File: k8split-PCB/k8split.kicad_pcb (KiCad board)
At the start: 2 copper layers, 421.6 x 118.7 mm, 233 parts, among them J1 AVR-ISP-6, J13 Breakaway_Tabs, J14 Breakaway_Tabs, J17 Breakaway_Tabs, J18 Breakaway_Tabs, J19 Breakaway_Tabs, J2 AVR-ISP-6, J3 Breakaway_Tabs, J5 Breakaway_Tabs, J6 Breakaway_Tabs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

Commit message: near completed routing on boards
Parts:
- added C6: 0.1uF, Capacitor_SMD:C_0603_1608Metric, B.Cu at (38.1, 129.5)
- added H1: MountingHole, MountingHole:MountingHole_3.2mm_M3, F.Cu at (-61.5, 29.0)
- added H2: MountingHole, MountingHole:MountingHole_3.2mm_M3, F.Cu at (-61.5, 140.7)
- added H3: MountingHole, MountingHole:MountingHole_3.2mm_M3, F.Cu at (88.4, 29.0)
- added H4: MountingHole, MountingHole:MountingHole_3.2mm_M3, F.Cu at (127.5, 140.7)
- added H5: MountingHole, MountingHole:MountingHole_3.2mm_M3, F.Cu at (203.7, 29.0)
- added H6: MountingHole, MountingHole:MountingHole_3.2mm_M3, F.Cu at (164.6, 140.7)
- added H7: MountingHole, MountingHole:MountingHole_3.2mm_M3, F.Cu at (353.6, 29.0)
- added H8: MountingHole, MountingHole:MountingHole_3.2mm_M3, F.Cu at (353.6, 140.7)
- C15, C3, C4, C7: moved to B.Cu
- moved C3 111.7 mm to (19.2, 132.6), turned to 90 degrees
- moved C4 108.8 mm to (26.4, 140.2)
- moved Y1 105.4 mm to (29.0, 122.4), turned to 180 degrees
- moved C7 104.7 mm to (26.4, 125.0), turned to 180 degrees
- moved C1 104.1 mm to (32.0, 122.4), turned to 90 degrees
- moved R25 103.8 mm to (38.1, 137.2), turned to 180 degrees
- moved C2 103.1 mm to (29.0, 119.9)
- moved C15 102.9 mm to (33.0, 140.2)
- moved C9 28.5 mm to (221.5, 120.9), turned to 270 degrees
- moved Y2 22.4 mm to (224.5, 120.9), turned to 180 degrees
- moved C8 16.3 mm to (227.6, 120.9), turned to 90 degrees
- moved D43 5.97 mm to (79.8, 29.8)
- moved R1 4.83 mm to (115.8, 107.2)
- moved SW1 3.09 mm to (120.0, 114.7)
- moved J1 3.09 mm to (120.0, 107.1)
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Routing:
- net GNDA: track 403.1 -> 9.36 mm, vias 8 -> 6
- net +5V: track 10.8 -> 323.5 mm, vias 0 -> 5
- net D-: track 0.00 -> 190.5 mm
- net D+: track 0.00 -> 189.7 mm
- net SCK: track 0.00 -> 124.1 mm, vias 0 -> 2
- net MISO: track 0.00 -> 119.7 mm, vias 0 -> 2
- net MOSI: track 0.00 -> 117.3 mm, vias 0 -> 2
- net RESET: track 8.23 -> 117.7 mm, vias 0 -> 3
- net ROW0: track 148.2 -> 253.2 mm, vias 0 -> 2
- net ROW1: track 133.3 -> 225.5 mm, vias 0 -> 2
- net COL0: track 103.1 -> 194.4 mm, vias 0 -> 1
- net COL7: track 111.2 -> 194.1 mm
- net ROW2: track 137.8 -> 212.1 mm, vias 0 -> 2
- net COL6: track 111.2 -> 178.6 mm, vias 0 -> 1
- net COL1: track 111.0 -> 178.3 mm, vias 0 -> 1
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- added copper zone on B.Cu, net GND
- added copper zone on F.Cu, net GND
- added copper zone on B.Cu, net GNDA
- added copper zone on F.Cu, net GNDA
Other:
- board size 421.6 x 118.7 mm -> 421.6 x 124.8 mm

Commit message: add some branding to pcb
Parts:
- added G***: LOGO, cad:pppp, B.Cu at (-58.6, 127.7)
- added G***: LOGO, cad:ppp, B.Cu at (350.9, 127.7)
- added G***: LOGO, cad:right, F.Cu at (291.6, 84.8)
- added G***: LOGO, cad:left, F.Cu at (0.51, 84.8)
- renumbered SW2 to RST, SW1 to RST
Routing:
- net Net-(D13-Pad2): track 0.00 -> 3.28 mm
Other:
- board text added: "https://github.com/ckath/k8split"

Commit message: small board redesign regarding usb, start fixing silkscreen
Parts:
- moved H1 2.54 mm to (-63.0, 26.9)
- moved G*** 2.30 mm to (-60.6, 128.9)
- moved H7 2.27 mm to (354.6, 26.9)
- moved H3 2.27 mm to (89.4, 26.9)
- moved H5 2.27 mm to (202.7, 26.9)
- moved H2 1.83 mm to (-63.0, 141.7)
- moved G*** 1.70 mm to (352.2, 128.8)
- moved H6 1.44 mm to (163.6, 141.7)
- moved H8 1.44 mm to (354.6, 141.7)
- moved H4 1.44 mm to (128.5, 141.7)
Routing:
- net D-: track 190.5 -> 191.3 mm
- net D+: track 189.7 -> 190.6 mm
- net GND: vias 4 -> 3
- net (no net): vias 0 -> 1
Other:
- board size 421.6 x 124.8 mm -> 424.7 x 121.9 mm
- board text added: "GITHUB.COM/CKATH/K8SPLIT"
- board text removed: "https://github.com/ckath/k8split"

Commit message: initial panelizing
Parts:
- removed J13, J14, J17, J18, J19: Breakaway_Tabs, locallib:breakaway-mousebites
- removed RST: SW_Push, locallib:SKQGADE010
- added J4: Breakaway_Tabs, locallib:breakaway-mousebites, F.Cu at (132.6, 142.0)
- added J8: Breakaway_Tabs, locallib:breakaway-mousebites, F.Cu at (89.7, 22.9)
- added SW2: SW_Push, locallib:SKQGADE010, F.Cu at (158.5, 79.4)
- moved J3 383.3 mm to (-43.7, 21.1)
- moved J5 212.0 mm to (108.5, 90.7), turned to 90 degrees
- moved J9 190.3 mm to (175.0, 22.6), turned to 180 degrees
- moved J6 184.9 mm to (147.6, 90.7), turned to 90 degrees
- moved J7 149.1 mm to (308.9, 20.8)
- moved G*** 34.0 mm to (257.6, 84.8)
- moved C10 27.4 mm to (188.5, 132.6)
- moved C11 27.4 mm to (193.0, 140.2)
- moved C16 27.4 mm to (200.2, 140.2)
- moved C8 27.4 mm to (200.2, 120.9)
- moved D49 27.4 mm to (190.4, 29.8)
- moved D52 27.4 mm to (166.2, 87.6)
- moved D53 27.4 mm to (156.7, 106.7)
- moved D54 27.4 mm to (152.3, 125.7)
- moved D56 27.4 mm to (190.4, 48.9)
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- renumbered RST to SW1
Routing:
- net SCK: track 124.1 -> 125.3 mm
- net GNDA: track 9.36 -> 10.4 mm
- net GND: vias 3 -> 5
- net (no net): vias 1 -> 0
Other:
- board size 424.7 x 121.9 mm -> 397.3 x 131.3 mm
- board text added: "JLCJLCJLCJLC"
- board text added: "rev 0.1"

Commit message: finish panelizing pcb
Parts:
- moved J7 160.6 mm to (151.6, 53.3), turned to 270 degrees
- moved J3 141.1 mm to (93.7, 53.3), turned to 90 degrees
- moved J9 5.75 mm to (170.9, 26.7), turned to 270 degrees
- moved J8 5.57 mm to (93.7, 26.7), turned to 90 degrees
- moved J6 0.51 mm to (147.1, 90.7), turned to 270 degrees
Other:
- board size 397.3 x 131.3 mm -> 397.3 x 124 mm
- board text added: "K 8 S P L I T R0.1"
- board text added: "initial release"

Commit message: initial gerber files
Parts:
- moved R67 2.40 mm to (204.7, 138.9)
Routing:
- net COL7-R: track 230.9 -> 229.6 mm
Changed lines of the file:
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@@
   (general
     (thickness 1.6)
-    (drawings 58)
-    (tracks 1130)
+    (drawings 60)
+    (tracks 1133)
     (zones 0)
     (modules 243)
@@
       (drillshape 0)
       (scaleselection 1)
-      (outputdirectory "Position"))
+      (outputdirectory "Gerber"))
   )
   (net 0 "")
@@
   )
   (module Resistor_SMD:R_0805_2012Metric (layer B.Cu)
-    (at 202.692 140.208 90)
+    (at 204.724 138.938 90)
     (descr "Resistor SMD 0805 (2012 Metric), square (rectangular) end terminal, IPC_7351 nominal, (Body size source: https://docs.google.com/spreadsheets/d/1BsfQQcO9C6DZCsRaXUlFlo91Tg2WpOkGARC1WS5S8t0/edit?usp=sharing), generated with kicad-footprint-generator")
     (tags resistor)
     (attr smd)
-    (fp_text reference R67 (at -2.54 0.508 180) (layer B.SilkS)
+    (fp_text reference R67 (at -2.54 0 180) (layer B.SilkS)
       (effects (font (size 1 1) (thickness 0.15)) (justify mirror))
     )
@@
   (module locallib:SKQGADE010 (layer F.Cu)
     (at 158.496 79.375)
-    (fp_text reference SW2 (at 0 4.064) (layer F.SilkS)
+    (fp_text reference SW2 (at 0 4.064) (layer F.SilkS) hide
       (effects (font (size 1 1) (thickness 0.15)))
     )
@@
   (module locallib:SKQGADE010 (layer F.Cu)
     (at 120.015 114.681)
-    (fp_text reference SW1 (at 0 3.81) (layer F.SilkS)
+    (fp_text reference SW1 (at 0 3.81) (layer F.SilkS) hide
       (effects (font (size 1 1) (thickness 0.15)))
     )
@@
     )
   )
+  (dimension 123.952 (width 0.15) (layer Dwgs.User)
+    (gr_text "123.952 mm" (at 342.422 83.312 90) (layer Dwgs.User)
+      (effects (font (size 1 1) (thickness 0.15)))
+    )
+    (feature1 (pts (xy 330.708 21.336) (xy 341.708421 21.336)))
+    (feature2 (pts (xy 330.708 145.288) (xy 341.708421 145.288)))
+    (crossbar (pts (xy 341.122 145.288) (xy 341.122 21.336)))
+    (arrow1a (pts (xy 341.122 21.336) (xy 341.708421 22.462504)))
+    (arrow1b (pts (xy 341.122 21.336) (xy 340.535579 22.462504)))
+    (arrow2a (pts (xy 341.122 145.288) (xy 341.708421 144.161496)))
+    (arrow2b (pts (xy 341.122 145.288) (xy 340.535579 144.161496)))
+  )
+  (dimension 397.256 (width 0.15) (layer Dwgs.User)
+    (gr_text "397.256 mm" (at 132.08 6.574001) (layer Dwgs.User)
+      (effects (font (size 1 1) (thickness 0.15)))
+    )
+    (feature1 (pts (xy -66.548 23.368) (xy -66.548 7.28758)))
+    (feature2 (pts (xy 330.708 23.368) (xy 330.708 7.28758)))
+    (crossbar (pts (xy 330.708 7.874001) (xy -66.548 7.874001)))
+    (arrow1a (pts (xy -66.548 7.874001) (xy -65.421496 7.28758)))
+    (arrow1b (pts (xy -66.548 7.874001) (xy -65.421496 8.460422)))
+    (arrow2a (pts (xy 330.708 7.874001) (xy 329.581496 7.28758)))
+    (arrow2b (pts (xy 330.708 7.874001) (xy 329.581496 8.460422)))
+  )
   (gr_text "initial release" (at 122.174 53.34) (layer F.SilkS)
     (effects (font (size 4 4) (thickness 0.5)))
@@
   (via (at 202.692 120.396) (size 0.8) (drill 0.4) (layers F.Cu B.Cu) (net 6))
   (via (at 195.58 123.444) (size 0.8) (drill 0.4) (layers F.Cu B.Cu) (net 6))
-  (via (at 204.216 140.208) (size 0.8) (drill 0.4) (layers F.Cu B.Cu) (net 6))
+  (via (at 203.708 141.478) (size 0.8) (drill 0.4) (layers F.Cu B.Cu) (net 6))
   (segment (start 188.1325 133.515) (end 189.892 133.515) (width 0.381) (layer B.Cu) (net 6))
   (segment (start 187.6805 133.063) (end 188.1325 133.515) (width 0.381) (layer B.Cu) (net 6))
@@
   (segment (start 304.416363 53.373325) (end 304.416363 67.681671) (width 0.254) (layer F.Cu) (net 140) (status 10))
   (segment (start 297.253524 117.720258) (end 309.102442 129.569176) (width 0.254) (layer F.Cu) (net 140) (status 20))
-  (segment (start 292.1 139.192) (end 205.232 139.192) (width 0.254) (layer B.Cu) (net 140))
   (segment (start 301.722824 129.569176) (end 309.102442 129.569176) (width 0.254) (layer B.Cu) (net 140) (status 20))
   (segment (start 292.1 139.192) (end 301.722824 129.569176) (width 0.254) (layer B.Cu) (net 140))
   (via (at 204.216 130.302) (size 0.8) (drill 0.4) (layers F.Cu B.Cu) (net 140))
-  (segment (start 204.203 130.315) (end 204.216 130.302) (width 0.254) (layer B.Cu) (net 140))
-  (segment (start 202.423 130.315) (end 204.203 130.315) (width 0.254) (layer B.Cu) (net 140) (status 10))
-  (segment (start 204.216 130.302) (end 204.216 138.176) (width 0.254) (layer F.Cu) (net 140))
-  (segment (start 204.216 138.176) (end 205.232 139.192) (width 0.254) (layer F.Cu) (net 140))
-  (via (at 205.232 139.192) (size 0.8) (drill 0.4) (layers F.Cu B.Cu) (net 140))
+  (via (at 204.978 136.144) (size 0.8) (drill 0.4) (layers F.Cu B.Cu) (net 140))
+  (segment (start 208.026 139.192) (end 204.978 136.144) (width 0.254) (layer B.Cu) (net 140))
+  (segment (start 292.1 139.192) (end 208.026 139.192) (width 0.254) (layer B.Cu) (net 140))
+  (segment (start 202.436 130.302) (end 202.423 130.315) (width 0.254) (layer B.Cu) (net 140))
+  (segment (start 204.216 130.302) (end 202.436 130.302) (width 0.254) (layer B.Cu) (net 140))
+  (segment (start 204.578001 135.744001) (end 204.978 136.144) (width 0.254) (layer F.Cu) (net 140))
+  (segment (start 203.816001 130.701999) (end 203.816001 134.982001) (width 0.254) (layer F.Cu) (net 140))
+  (segment (start 203.816001 134.982001) (end 204.578001 135.744001) (width 0.254) (layer F.Cu) (net 140))
+  (segment (start 204.216 130.302) (end 203.816001 130.701999) (width 0.254) (layer F.Cu) (net 140))
   (segment (start -44.744 32.0425) (end -44.704 32.0825) (width 0.254) (layer B.Cu) (net 141) (status 30))
   (segment (start -44.744 29.464) (end -44.744 32.0425) (width 0.254) (layer B.Cu) (net 141) (status 30))
@@
   (segment (start 36.5905 136.588) (end 37.1625 137.16) (width 0.254) (layer B.Cu) (net 147) (status 20))
   (segment (start 35.418 136.588) (end 36.5905 136.588) (width 0.254) (layer B.Cu) (net 147) (status 10))
-  (segment (start 202.423 139.0015) (end 202.692 139.2705) (width 0.254) (layer B.Cu) (net 148) (status 30))
-  (segment (start 202.423 136.715) (end 202.423 139.0015) (width 0.254) (layer B.Cu) (net 148) (status 30))
+  (segment (start 203.4385 136.715) (end 202.423 136.715) (width 0.254) (layer B.Cu) (net 148))
+  (segment (start 204.724 138.0005) (end 203.4385 136.715) (width 0.254) (layer B.Cu) (net 148))
   (segment (start 253.893267 69.595) (end 253.594201 69.894066) (width 0.254) (layer B.Cu) (net 167) (status 30))
   (segment (start 257.048 69.595) (end 253.893267 69.595) (width 0.254) (layer B.Cu) (net 167) (status 30))

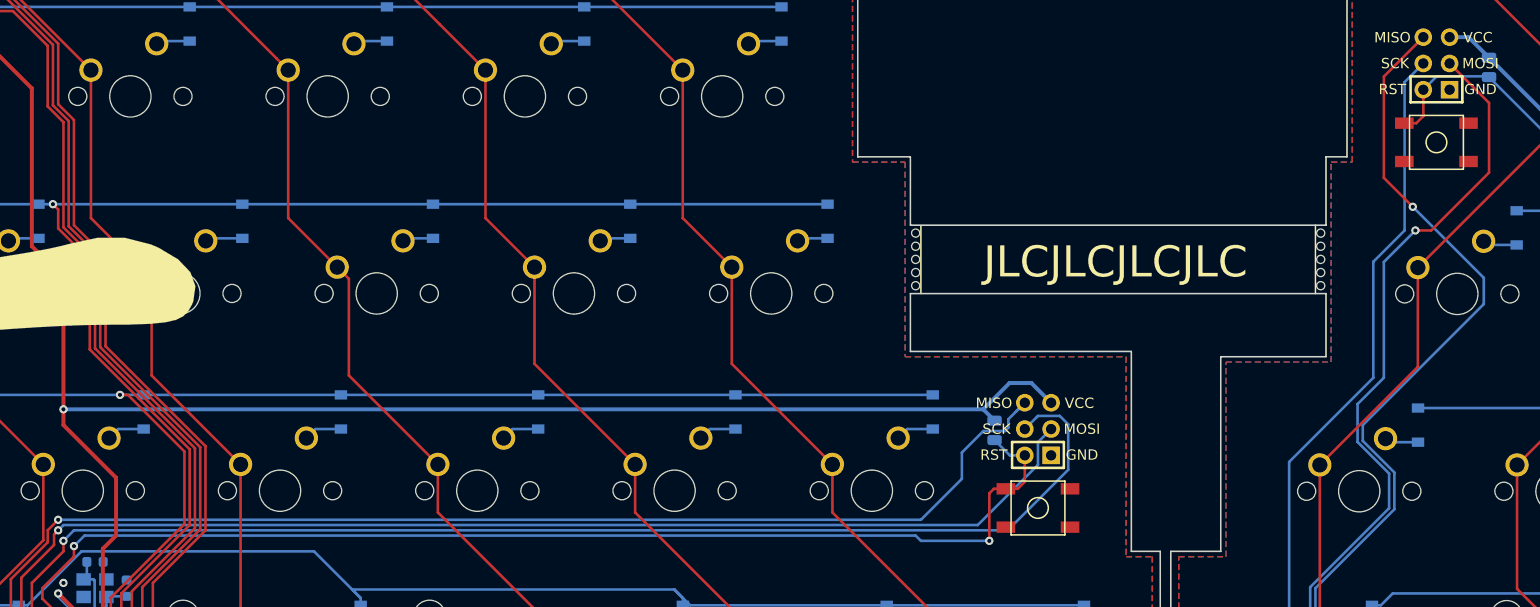
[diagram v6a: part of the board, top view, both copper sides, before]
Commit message: add jlc bom, move switches
- all part numbers found on jlc, might change some packages later
- move switches to other side because smd manufacturing is one side
- gerbers not regenerated, more changes to be done before doing it again
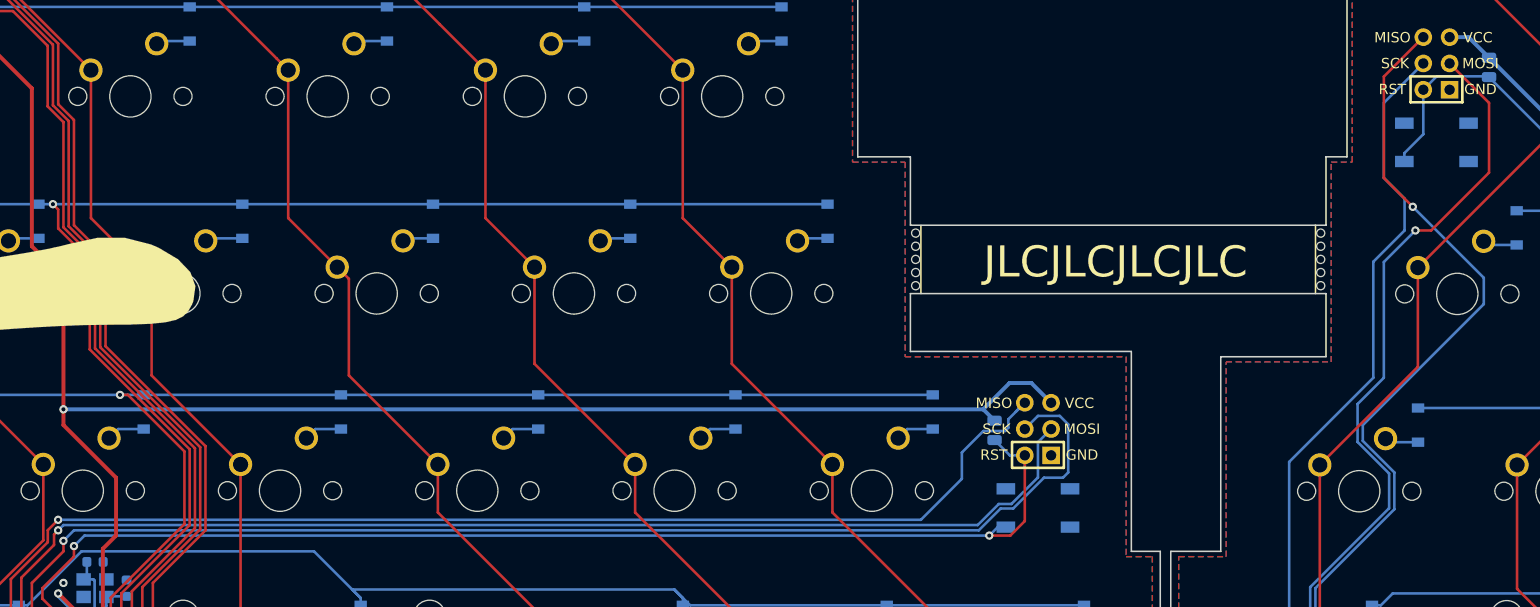
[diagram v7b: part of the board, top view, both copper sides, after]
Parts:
- SW1, SW2: moved to B.Cu
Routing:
- net RESET-R: track 104.7 -> 107.7 mm
- net RESET: track 117.7 -> 120.0 mm
- net SCK-R: track 118.2 -> 119.8 mm
- net MOSI: track 117.6 -> 118.3 mm

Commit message: cleaned up libs and parts
- switched out 0805 resistors to 0603
- deleted some unused libraries
- re-associated symbols libs to point to system ones
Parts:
- R1, R2, R25, R3, R4, R5, R6, R67: footprint Resistor_SMD:R_0805_2012Metric -> Resistor_SMD:R_0603_1608Metric
- moved R67 0.57 mm to (204.2, 138.7)
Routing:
- net +5V: track 323.5 -> 327.4 mm
- net ROW0: track 253.2 -> 254.3 mm
- net R-D+: track 255.0 -> 255.7 mm
